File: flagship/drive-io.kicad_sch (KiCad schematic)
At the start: 12 parts, among them U10 74AHCT125, U9 THVD1450

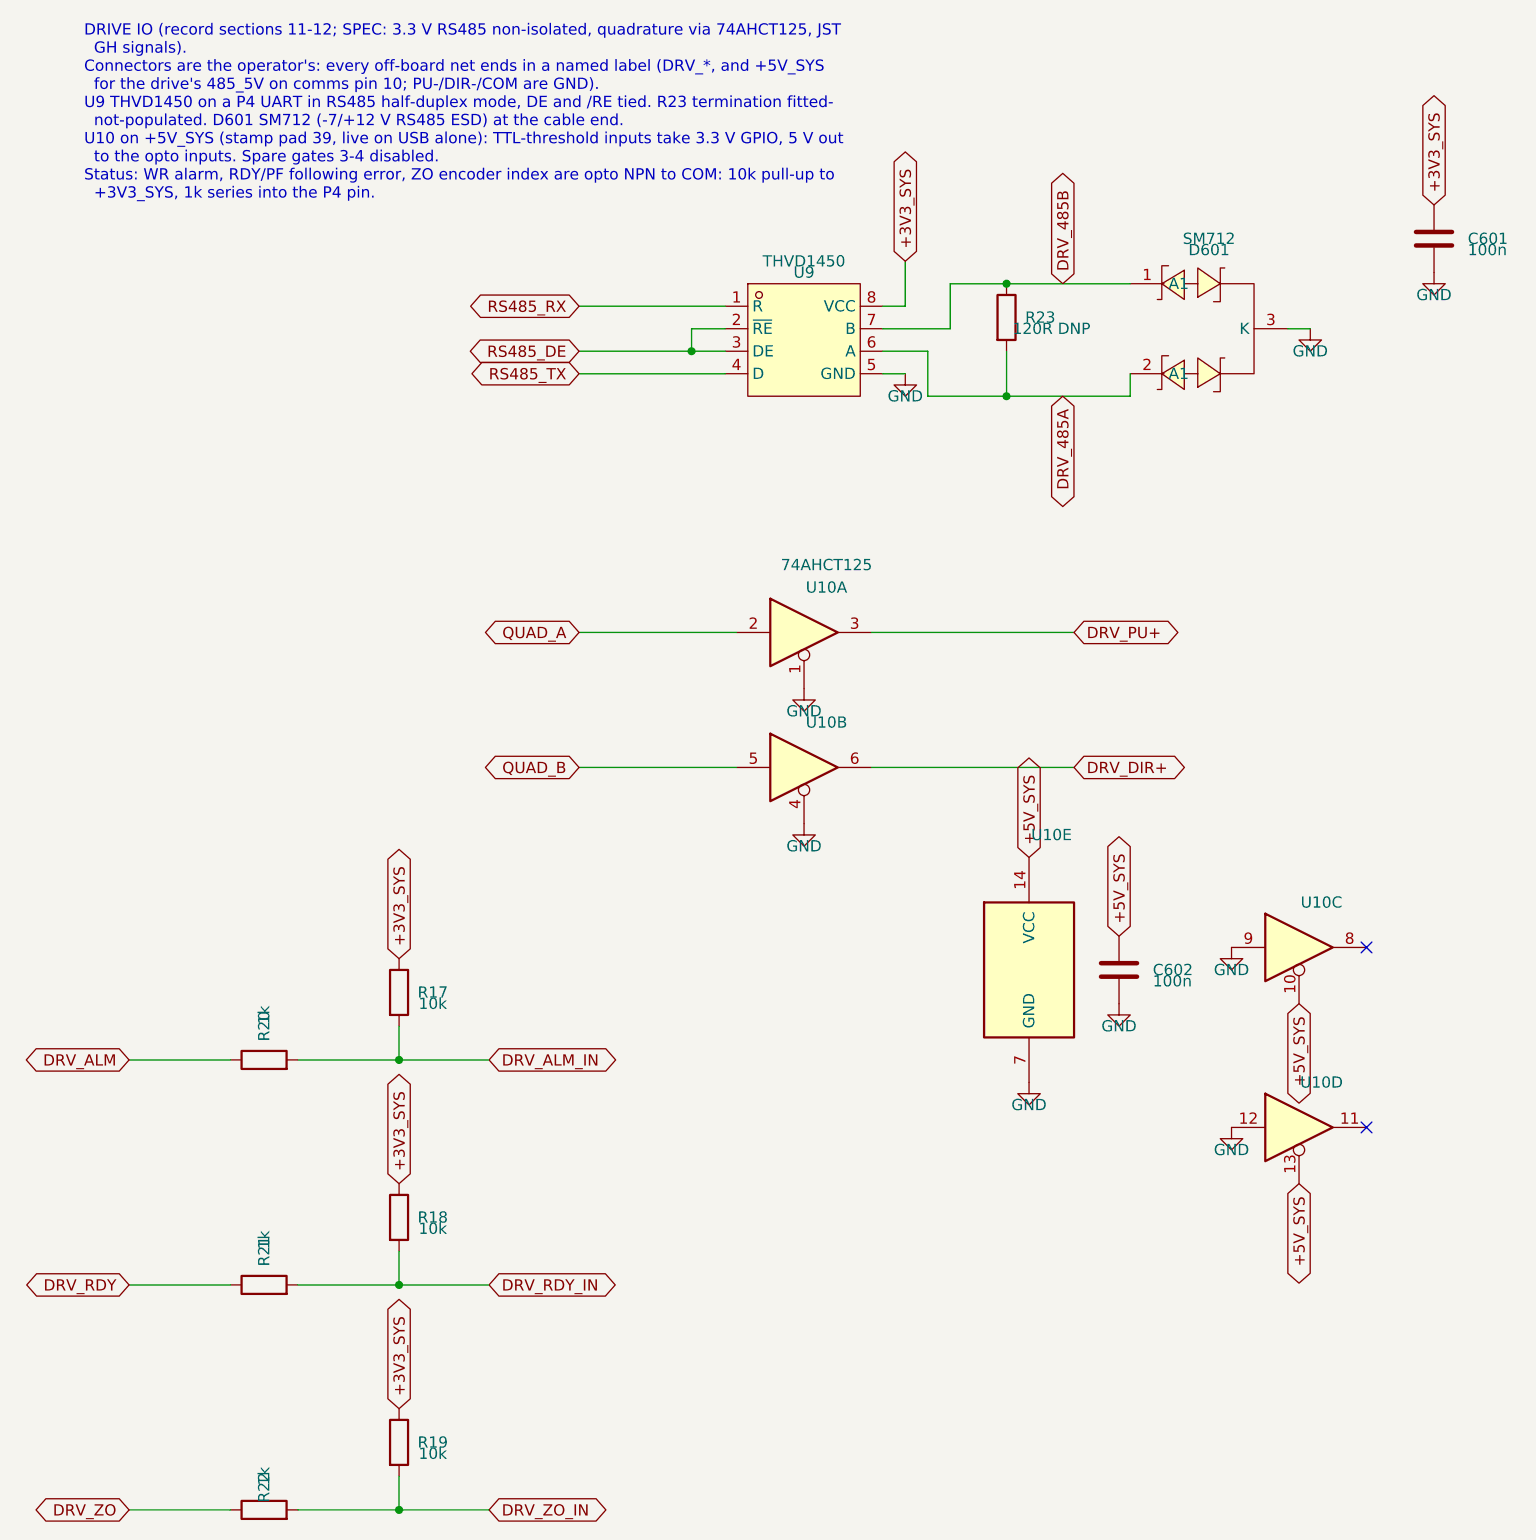
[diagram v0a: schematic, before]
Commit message: flagship: drive connectors (XT30 + GH4 motion / XT30 ext shunt + GH6 comms), HOME and PAIR buttons with EN/BOOT rescue pads, status LED through AHCT125 gate 3, ZO dropped; FEATURES.md
ZO removal: DRV_ZO / DRV_ZO_IN and R19/R22 existed only on the Drive IO sheet (netlist checked: no other node on either net).
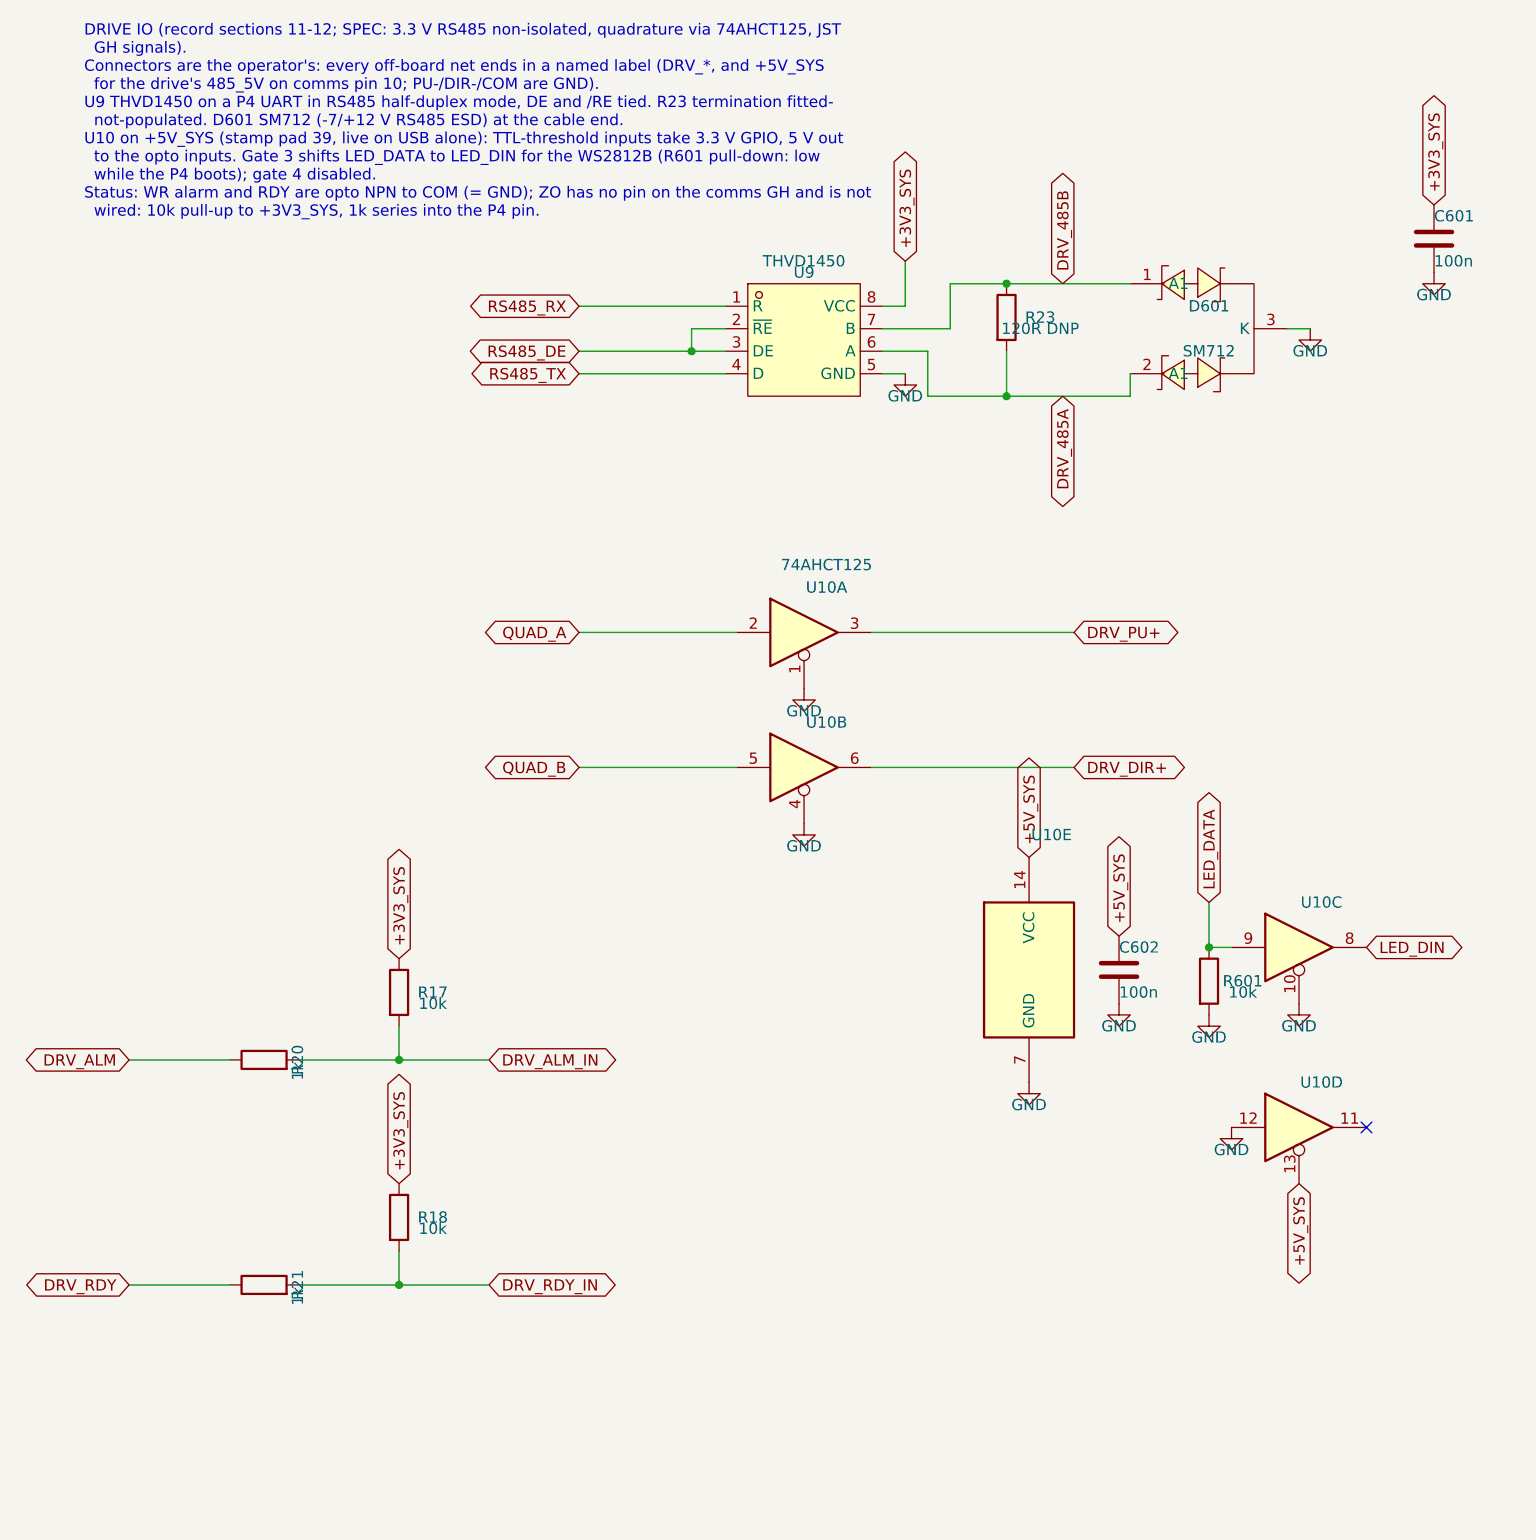
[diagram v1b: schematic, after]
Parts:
- removed R19: 10k, Resistor_SMD:R_0805_2012Metric, symbol Device:R
- removed R22: 1k, Resistor_SMD:R_0805_2012Metric, symbol Device:R
- added R601: 10k, Resistor_SMD:R_0805_2012Metric, symbol Device:R
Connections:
- net +5V_SYS: no longer U10.10
- net GND: now also U10.10, R601.2; no longer U10.9
- net LED_DIN: now reaches U10.8
- new net LED_DATA: R601.1, U10.9
- no-connect marks 2 -> 1
